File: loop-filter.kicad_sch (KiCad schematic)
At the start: 0 parts

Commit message: Complete Schematic of the PCB
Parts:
- added C19, C24: 1uF, Package_SO:SOIC-8_3.9x4.9mm_P1.27mm, symbol Device:C
- added C20: 96.5pF, Package_SO:SOIC-8_3.9x4.9mm_P1.27mm, symbol Device:C
- added C21: 215pF, Package_SO:SOIC-8_3.9x4.9mm_P1.27mm, symbol Device:C
- added C22: 739pF, Package_SO:SOIC-8_3.9x4.9mm_P1.27mm, symbol Device:C
- added C23: 25.9pF, Package_SO:SOIC-8_3.9x4.9mm_P1.27mm, symbol Device:C
- added R26, R27: 47k, symbol Device:R_US
- added R28: 220, symbol Device:R_US
- added R29: 1k, symbol Device:R_US
- added R30: 2.55k, symbol Device:R_US
- added U6: RRA78610-QAJ, Package_TO_SOT_SMD:SOT-353_SC-70-5, symbol Custom Symbols:RRA78610-QAJ_Op_Amp
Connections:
- new net: C19.1, R26.2, R27.1, U6.1 (IN+)
- new net: C23.2, R28.2, R30.1, U6.3 (IN-)
- new net: C22.1, C23.1, R29.1, U6.4 (OUT)
- new net: C22.2, R30.2
- new net 3.0V: R26.1
- new net 5.5V: C24.1, U6.5 (V+)
- new net CPOUT: C20.2, R28.1
- new net GND: C19.2, C20.1, C21.1, C24.2, R27.2, U6.2 (V-)
- new net VTUNE: C21.2, R29.2
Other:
- title: (none) -> Fifth-order Loop Filter with 4 poles

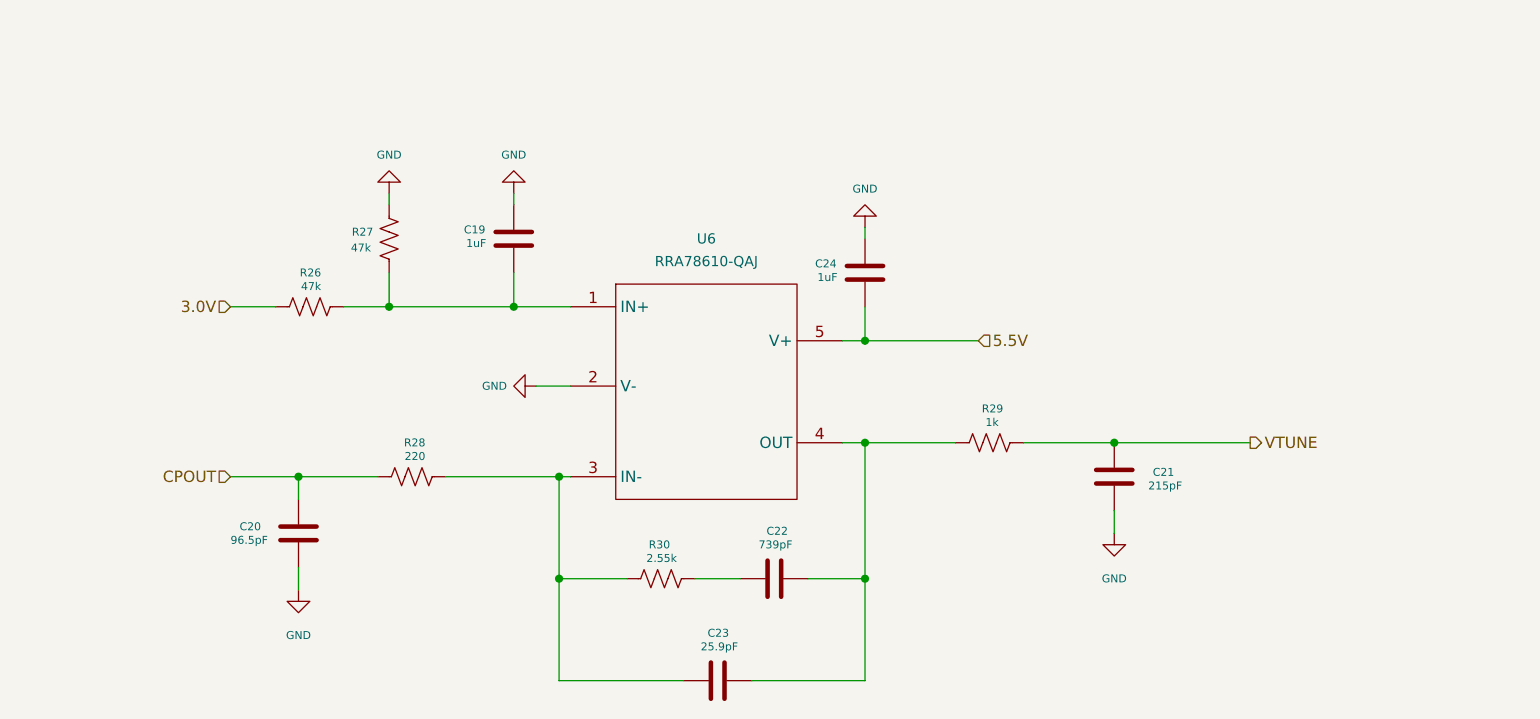
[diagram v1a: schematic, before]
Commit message: Remove 0ohm resistors for EN pins and SMA connector for external REFIN
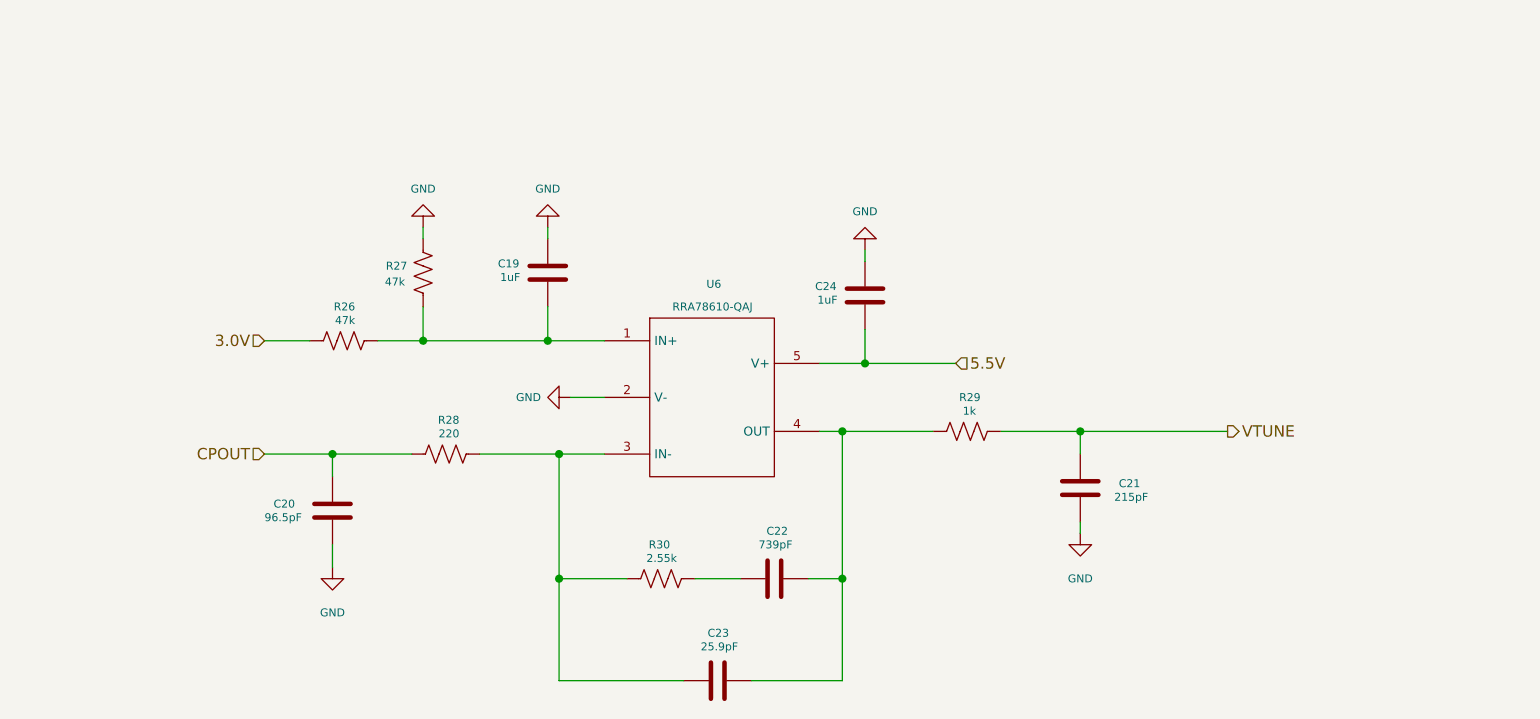
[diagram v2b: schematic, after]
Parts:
- removed U6: RRA78610-QAJ, Package_TO_SOT_SMD:SOT-353_SC-70-5, symbol Custom Symbols:RRA78610-QAJ_Op_Amp
- added U6: RRA78610-QAJ, Package_TO_SOT_SMD:SOT-353_SC-70-5, symbol Custom_Library:RRA78610-QAJ
- C19, C20, C21, C22, C23, C24: footprint Package_SO:SOIC-8_3.9x4.9mm_P1.27mm -> Capacitor_SMD:C_0402_1005Metric
- R26, R27, R28, R29, R30: footprint (none) -> Capacitor_SMD:C_0402_1005Metric
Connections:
- net 5.5V: now also U6.5 (V+)
- net GND: now also U6.2 (V-)
- net at C19.1, R26.2, R27.1: now also U6.1 (IN+)
- net at C23.2, R28.2, R30.1: now also U6.3 (IN-)
- net at C22.1, C23.1, R29.1: now also U6.4 (OUT)
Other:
- moved on the sheet: C19, C20, C21, C24, R26, R27, R28, R29

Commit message: Complete and adjust the PCB based on advisor's advice and manufacturer in-stock parts
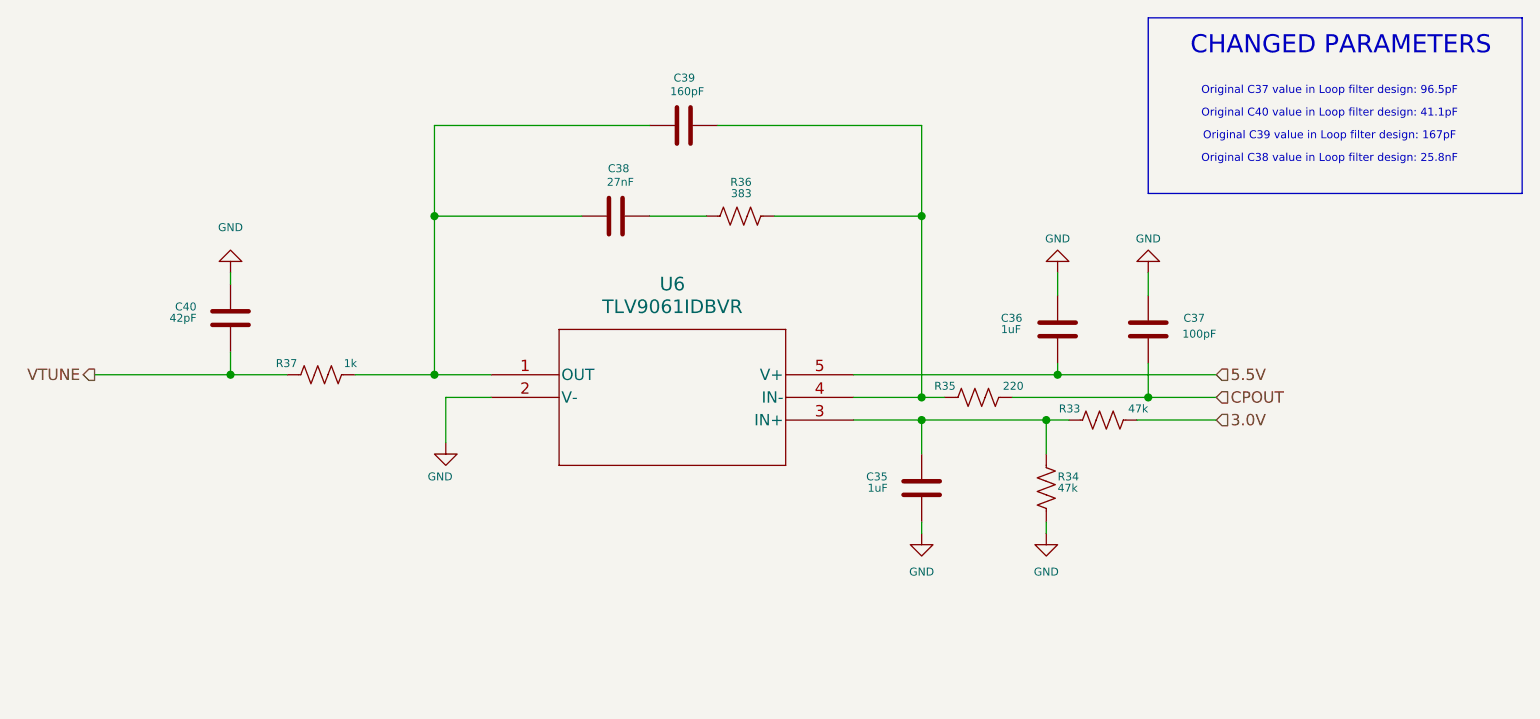
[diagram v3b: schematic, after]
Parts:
- removed C19, C24: 1uF, Capacitor_SMD:C_0402_1005Metric, symbol Device:C
- removed C20: 96.5pF, Capacitor_SMD:C_0402_1005Metric, symbol Device:C
- removed C21: 215pF, Capacitor_SMD:C_0402_1005Metric, symbol Device:C
- removed C22: 739pF, Capacitor_SMD:C_0402_1005Metric, symbol Device:C
- removed C23: 25.9pF, Capacitor_SMD:C_0402_1005Metric, symbol Device:C
- removed R26, R27: 47k, Capacitor_SMD:C_0402_1005Metric, symbol Device:R_US
- removed R28: 220, Capacitor_SMD:C_0402_1005Metric, symbol Device:R_US
- removed R29: 1k, Capacitor_SMD:C_0402_1005Metric, symbol Device:R_US
- removed R30: 2.55k, Capacitor_SMD:C_0402_1005Metric, symbol Device:R_US
- removed U6: RRA78610-QAJ, Package_TO_SOT_SMD:SOT-353_SC-70-5, symbol Custom_Library:RRA78610-QAJ
- added C35, C36: 1uF, Capacitor_SMD:C_0402_1005Metric, symbol Device:C
- added C37: 100pF, Capacitor_SMD:C_0402_1005Metric, symbol Device:C
- added C38: 27nF, Capacitor_SMD:C_0402_1005Metric, symbol Device:C
- added C39: 160pF, Capacitor_SMD:C_0402_1005Metric, symbol Device:C
- added C40: 42pF, Capacitor_SMD:C_0603_1608Metric, symbol Device:C
- added R33, R34: 47k, Resistor_SMD:R_0402_1005Metric, symbol Device:R_US
- added R35: 220, Resistor_SMD:R_0402_1005Metric, symbol Device:R_US
- added R36: 383, Resistor_SMD:R_0402_1005Metric, symbol Device:R_US
- added R37: 1k, Resistor_SMD:R_0402_1005Metric, symbol Device:R_US
- added U6: TLV9061IDBVR, symbols:DBV5_TEX, symbol TLV9061IDBVR:TLV9061IDBVR
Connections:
- net 3.0V: now also R33.2
- net 5.5V: now also C36.1, U6.5 (V+)
- net CPOUT: now also C37.2, R35.2
- net GND: now also C35.2, C36.2, C37.1, C40.1, R34.2, U6.2 (V-)
- net VTUNE: now also C40.2, R37.2
- new net: C39.1, R35.1, R36.2, U6.4 (IN-)
- new net: C38.2, C39.2, R37.1, U6.1 (OUT)
- new net: C38.1, R36.1
- new net: C35.1, R33.1, R34.1, U6.3 (IN+)
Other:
- note added: "CHANGED PARAMETERS"
- note added: "Original C37 value in Loop filter design: 96.5pF"
- note added: "Original C38 value in Loop filter design: 25.8nF"
- note added: "Original C39 value in Loop filter design: 167pF"
- note added: "Original C40 value in Loop filter design: 41.1pF"
